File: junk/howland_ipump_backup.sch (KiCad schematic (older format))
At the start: 13 parts, among them Q1 BC856, U11 OPA991S

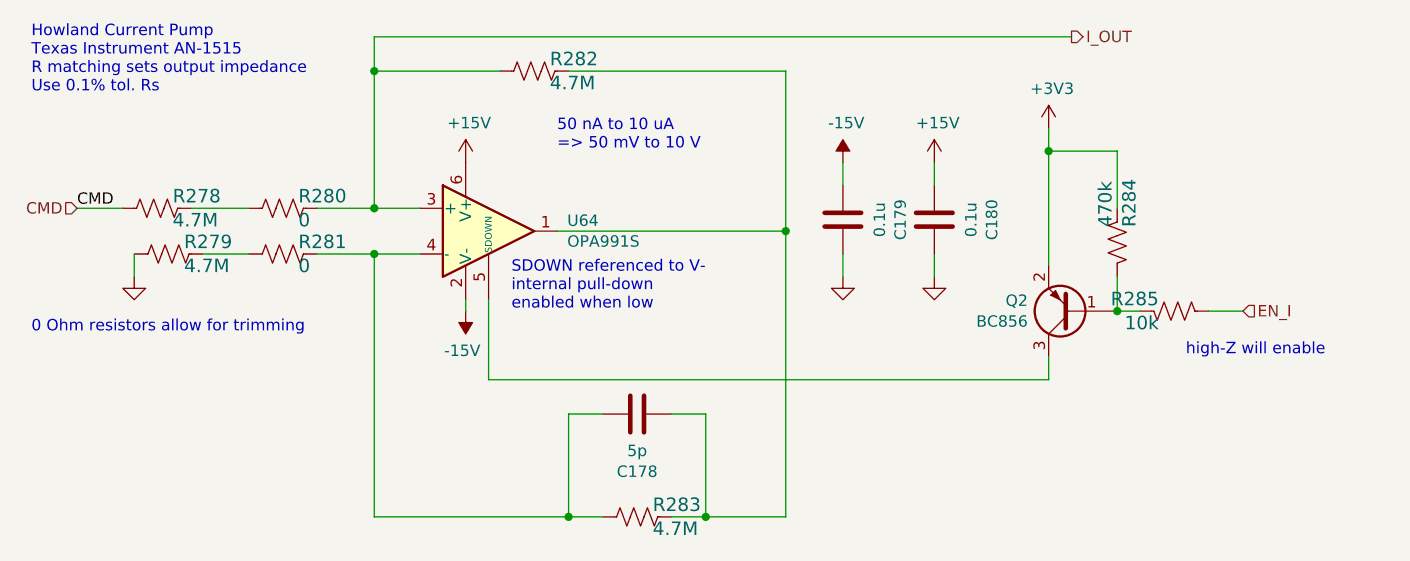
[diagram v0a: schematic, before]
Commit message: changed 0.1uF cap to Samsung
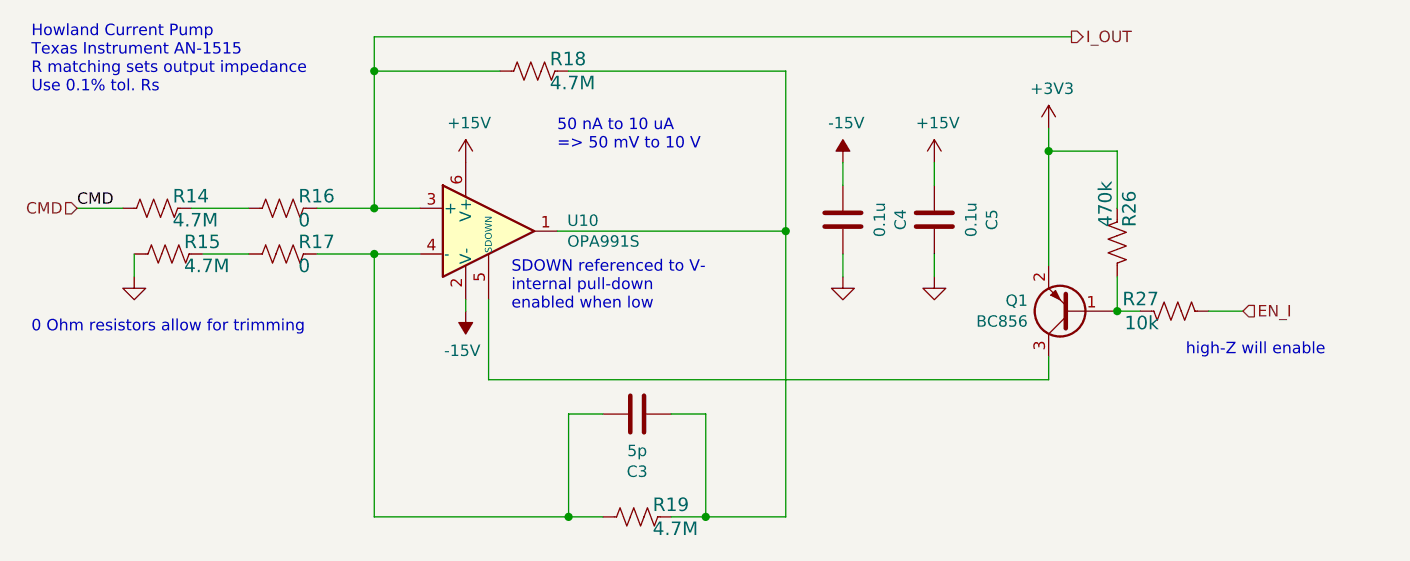
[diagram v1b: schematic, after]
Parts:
- C34, C35: Manf# CL10B104KA8NFNC -> CC0603MRX7R8BB104; Manufacturer_Name Samsung -> Yageo; Tolerance 10% -> 20%
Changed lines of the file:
@@
 $Descr A4 11693 8268
 encoding utf-8
-Sheet 18 18
+Sheet 3 18
 Title ""
 Date ""
@@
 AR Path="/6095BD4C/60C5A41E/60D781E3" Ref="#PWR?"  Part="1"
 AR Path="/61B02572/60BE01FC/60D781E3" Ref="#PWR0331"  Part="1"
-F 0 "#PWR0331" H 5100 4150 50  0001 C CNN
+F 0 "#PWR0116" H 5100 4150 50  0001 C CNN
 F 1 "-15V" H 5115 4223 50  0000 C CNN
 F 2 "" H 5100 4050 50  0001 C CNN
@@
 AR Path="/6095BD4C/60C5A41E/60D781E9" Ref="#PWR?"  Part="1"
 AR Path="/61B02572/60BE01FC/60D781E9" Ref="#PWR0332"  Part="1"
-F 0 "#PWR0332" H 5100 3250 50  0001 C CNN
+F 0 "#PWR0157" H 5100 3250 50  0001 C CNN
 F 1 "+15V" H 5115 3573 50  0000 C CNN
 F 2 "" H 5100 3400 50  0001 C CNN
@@
 AR Path="/6095BD4C/60C5A41E/60D781F4" Ref="C?"  Part="1"
 AR Path="/61B02572/60BE01FC/60D781F4" Ref="C178"  Part="1"
-F 0 "C178" V 5598 4500 50  0000 C CNN
+F 0 "C3" V 5598 4500 50  0000 C CNN
 F 1 "5p" V 5689 4500 50  0000 C CNN
 F 2 "Capacitor_SMD:C_0603_1608Metric" H 5888 4350 50  0001 C CNN
@@
 AR Path="/6095BD4C/60C5A41E/60D78215" Ref="#PWR?"  Part="1"
 AR Path="/61B02572/60BE01FC/60D78215" Ref="#PWR0333"  Part="1"
-F 0 "#PWR0333" H 3650 3650 50  0001 C CNN
+F 0 "#PWR0158" H 3650 3650 50  0001 C CNN
 F 1 "GND" V 3655 3772 50  0001 R CNN
 F 2 "" H 3650 3900 50  0001 C CNN
@@
 AR Path="/6095BD4C/60C5A41E/60D7821F" Ref="U?"  Part="1"
 AR Path="/61B02572/60BE01FC/60D7821F" Ref="U64"  Part="1"
-F 0 "U64" H 5544 3746 50  0000 L CNN
+F 0 "U10" H 5544 3746 50  0000 L CNN
 F 1 "OPA991S" H 5544 3655 50  0000 L CNN
 F 2 "Package_TO_SOT_SMD:SOT-23-6" H 5350 3450 50  0001 L CNN
@@
 AR Path="/6095BD4C/60C5A41E/60D78240" Ref="R?"  Part="1"
 AR Path="/61B02572/60BE01FC/60D78240" Ref="R283"  Part="1"
-F 0 "R283" V 5797 5018 59  0000 L CNN
+F 0 "R19" V 5797 5018 59  0000 L CNN
 F 1 "4.7M" V 5902 5018 59  0000 L CNN
 F 2 "Resistor_SMD:R_1206_3216Metric" H 5850 4950 50  0001 C CNN
@@
 AR Path="/6095BD4C/60C5A41E/60D7824A" Ref="C?"  Part="1"
 AR Path="/61B02572/60BE01FC/60D7824A" Ref="C179"  Part="1"
-F 0 "C179" V 6498 3650 50  0000 C CNN
+F 0 "C4" V 6498 3650 50  0000 C CNN
 F 1 "0.1u" V 6589 3650 50  0000 C CNN
 F 2 "Capacitor_SMD:C_0603_1608Metric" H 6788 3500 50  0001 C CNN
 F 3 "~" H 6750 3650 50  0001 C CNN
-F 4 "CL10B104KA8NFNC" H 6498 3750 50  0001 C CNN "Manf#"
-F 5 "Samsung" H 6498 3750 50  0001 C CNN "Manufacturer_Name"
-F 6 "10%" H 6498 3750 50  0001 C CNN "Tolerance"
+F 4 "CC0603MRX7R8BB104" H 6498 3750 50  0001 C CNN "Manf#"
+F 5 "Yageo" H 6498 3750 50  0001 C CNN "Manufacturer_Name"
+F 6 "20%" H 6498 3750 50  0001 C CNN "Tolerance"
 F 7 "25" H 6498 3750 50  0001 C CNN "voltage"
 	1    6750 3650
@@
 AR Path="/6095BD4C/60C5A41E/60D78250" Ref="#PWR?"  Part="1"
 AR Path="/61B02572/60BE01FC/60D78250" Ref="#PWR0334"  Part="1"
-F 0 "#PWR0334" H 6750 3650 50  0001 C CNN
+F 0 "#PWR0163" H 6750 3650 50  0001 C CNN
 F 1 "GND" V 6755 3772 50  0001 R CNN
 F 2 "" H 6750 3900 50  0001 C CNN
@@
 AR Path="/6095BD4C/60C5A41E/60D78256" Ref="#PWR?"  Part="1"
 AR Path="/61B02572/60BE01FC/60D78256" Ref="#PWR0335"  Part="1"
-F 0 "#PWR0335" H 7150 3250 50  0001 C CNN
+F 0 "#PWR0164" H 7150 3250 50  0001 C CNN
 F 1 "+15V" H 7165 3573 50  0000 C CNN
 F 2 "" H 7150 3400 50  0001 C CNN
@@
 AR Path="/6095BD4C/60C5A41E/60D7825C" Ref="#PWR?"  Part="1"
 AR Path="/61B02572/60BE01FC/60D7825C" Ref="#PWR0336"  Part="1"
-F 0 "#PWR0336" H 7150 3650 50  0001 C CNN
+F 0 "#PWR0165" H 7150 3650 50  0001 C CNN
 F 1 "GND" V 7155 3772 50  0001 R CNN
 F 2 "" H 7150 3900 50  0001 C CNN
@@
 AR Path="/6095BD4C/60C5A41E/60D78264" Ref="C?"  Part="1"
 AR Path="/61B02572/60BE01FC/60D78264" Ref="C180"  Part="1"
-F 0 "C180" V 6898 3650 50  0000 C CNN
+F 0 "C5" V 6898 3650 50  0000 C CNN
 F 1 "0.1u" V 6989 3650 50  0000 C CNN
 F 2 "Capacitor_SMD:C_0603_1608Metric" H 7188 3500 50  0001 C CNN
 F 3 "~" H 7150 3650 50  0001 C CNN
-F 4 "CL10B104KA8NFNC" H 6898 3750 50  0001 C CNN "Manf#"
-F 5 "Samsung" H 6898 3750 50  0001 C CNN "Manufacturer_Name"
-F 6 "10%" H 6898 3750 50  0001 C CNN "Tolerance"
+F 4 "CC0603MRX7R8BB104" H 6898 3750 50  0001 C CNN "Manf#"
+F 5 "Yageo" H 6898 3750 50  0001 C CNN "Manufacturer_Name"
+F 6 "20%" H 6898 3750 50  0001 C CNN "Tolerance"
 F 7 "25" H 6898 3750 50  0001 C CNN "voltage"
 	1    7150 3650
@@
 AR Path="/6095BD4C/60C5A41E/60D7826A" Ref="#PWR?"  Part="1"
 AR Path="/61B02572/60BE01FC/60D7826A" Ref="#PWR0337"  Part="1"
-F 0 "#PWR0337" H 6750 3500 50  0001 C CNN
+F 0 "#PWR0166" H 6750 3500 50  0001 C CNN
 F 1 "-15V" H 6765 3573 50  0000 C CNN
 F 2 "" H 6750 3400 50  0001 C CNN
@@
 AR Path="/6095BD4C/60C5A41E/60D83006" Ref="R?"  Part="1"
 AR Path="/61B02572/60BE01FC/60D83006" Ref="R281"  Part="1"
-F 0 "R281" V 4247 3868 59  0000 L CNN
+F 0 "R17" V 4247 3868 59  0000 L CNN
 F 1 "0" V 4352 3868 59  0000 L CNN
 F 2 "Resistor_SMD:R_0603_1608Metric" H 4300 3800 50  0001 C CNN
@@
 AR Path="/6095BD4C/60C5A41E/60D8879F" Ref="R?"  Part="1"
 AR Path="/61B02572/60BE01FC/60D8879F" Ref="R280"  Part="1"
-F 0 "R280" V 4247 3668 59  0000 L CNN
+F 0 "R16" V 4247 3668 59  0000 L CNN
 F 1 "0" V 4352 3668 59  0000 L CNN
 F 2 "Resistor_SMD:R_0603_1608Metric" H 4300 3600 50  0001 C CNN
@@
 AR Path="/6095BD4C/60C5A41E/60B385AE" Ref="R?"  Part="1"
 AR Path="/61B02572/60BE01FC/60B385AE" Ref="R279"  Part="1"
-F 0 "R279" V 3747 3868 59  0000 L CNN
+F 0 "R15" V 3747 3868 59  0000 L CNN
 F 1 "4.7M" V 3852 3868 59  0000 L CNN
 F 2 "Resistor_SMD:R_1206_3216Metric" H 3800 3800 50  0001 C CNN
@@
 AR Path="/6095BD4C/60C5A41E/60B38EA4" Ref="R?"  Part="1"
 AR Path="/61B02572/60BE01FC/60B38EA4" Ref="R278"  Part="1"
-F 0 "R278" V 3697 3668 59  0000 L CNN
+F 0 "R14" V 3697 3668 59  0000 L CNN
 F 1 "4.7M" V 3802 3668 59  0000 L CNN
 F 2 "Resistor_SMD:R_1206_3216Metric" H 3750 3600 50  0001 C CNN
@@
 AR Path="/6095BD4C/60C5A41E/60B3940D" Ref="R?"  Part="1"
 AR Path="/61B02572/60BE01FC/60B3940D" Ref="R282"  Part="1"
-F 0 "R282" V 5347 3068 59  0000 L CNN
+F 0 "R18" V 5347 3068 59  0000 L CNN
 F 1 "4.7M" V 5452 3068 59  0000 L CNN
 F 2 "Resistor_SMD:R_1206_3216Metric" H 5400 3000 50  0001 C CNN
@@
 AR Path="/6095BD4C/60BE01FC/60BEDC00" Ref="Q1"  Part="1"
 AR Path="/61B02572/60BE01FC/60BEDC00" Ref="Q2"  Part="1"
-F 0 "Q2" H 7941 4004 50  0000 L CNN
+F 0 "Q1" H 7941 4004 50  0000 L CNN
 F 1 "BC856" H 7941 4095 50  0000 L CNN
 F 2 "Package_TO_SOT_SMD:SOT-23" H 7950 3975 50  0001 L CIN
@@
 AR Path="/6095BD4C/60C5A41E/60BF0E09" Ref="R?"  Part="1"
 AR Path="/61B02572/60BE01FC/60BF0E09" Ref="R285"  Part="1"
-F 0 "R285" V 8147 4118 59  0000 L CNN
+F 0 "R27" V 8147 4118 59  0000 L CNN
 F 1 "10k" V 8252 4118 59  0000 L CNN
 F 2 "Resistor_SMD:R_0603_1608Metric" H 8200 4050 50  0001 C CNN
@@
 AR Path="/6095BD4C/60BE01FC/60BF2F91" Ref="#PWR0160"  Part="1"
 AR Path="/61B02572/60BE01FC/60BF2F91" Ref="#PWR0338"  Part="1"
-F 0 "#PWR0338" H 7650 3100 50  0001 C CNN
+F 0 "#PWR0160" H 7650 3100 50  0001 C CNN
 F 1 "+3V3" H 7665 3423 50  0000 C CNN
 F 2 "" H 7650 3250 50  0001 C CNN
@@
 AR Path="/6095BD4C/60C5A41E/60C16A39" Ref="R?"  Part="1"
 AR Path="/61B02572/60BE01FC/60C16A39" Ref="R284"  Part="1"
-F 0 "R284" V 7897 3818 59  0000 L CNN
+F 0 "R26" V 7897 3818 59  0000 L CNN
 F 1 "470k" V 8002 3818 59  0000 L CNN
 F 2 "Resistor_SMD:R_0603_1608Metric" H 7950 3750 50  0001 C CNN
